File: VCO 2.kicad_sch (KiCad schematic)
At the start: 84 parts, among them J1 OUT 1x4s, J16 OCT_SW 1x7s, J18 CV 1x6s, J20 CTRL 1x9s, J85 Eurorack 2x8hs, J9 IN 1x6s, Q1 2N3904, Q2 2N3904, U1 CEM3340, U2 TL074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

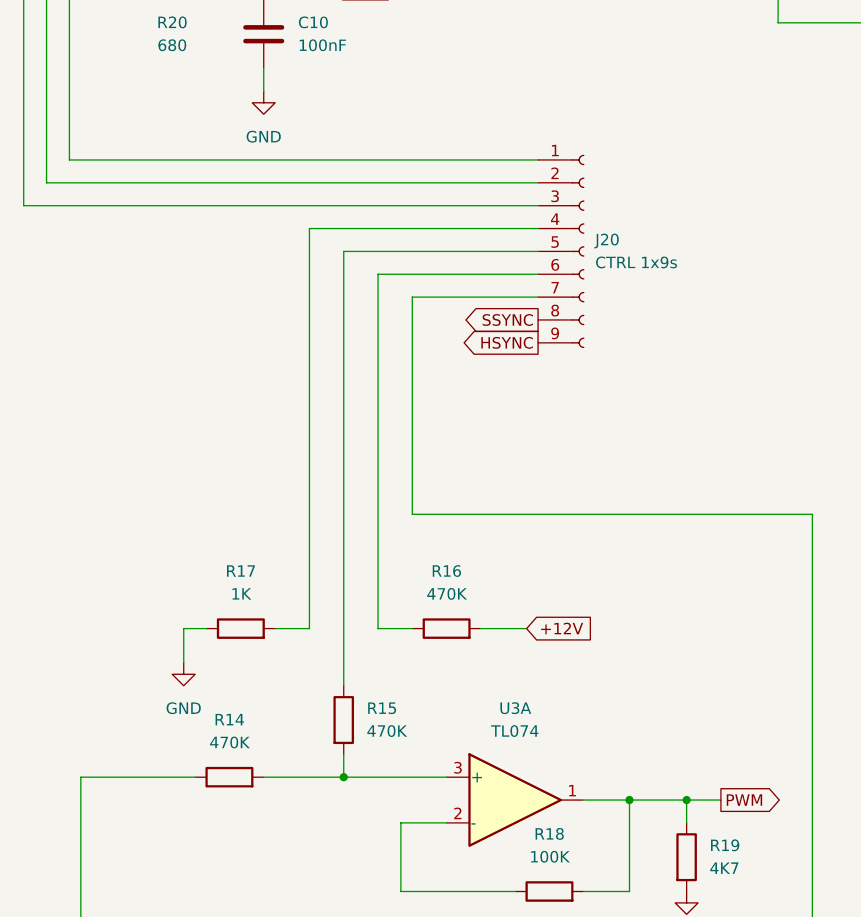
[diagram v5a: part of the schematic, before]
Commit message: Fixed FM sweep
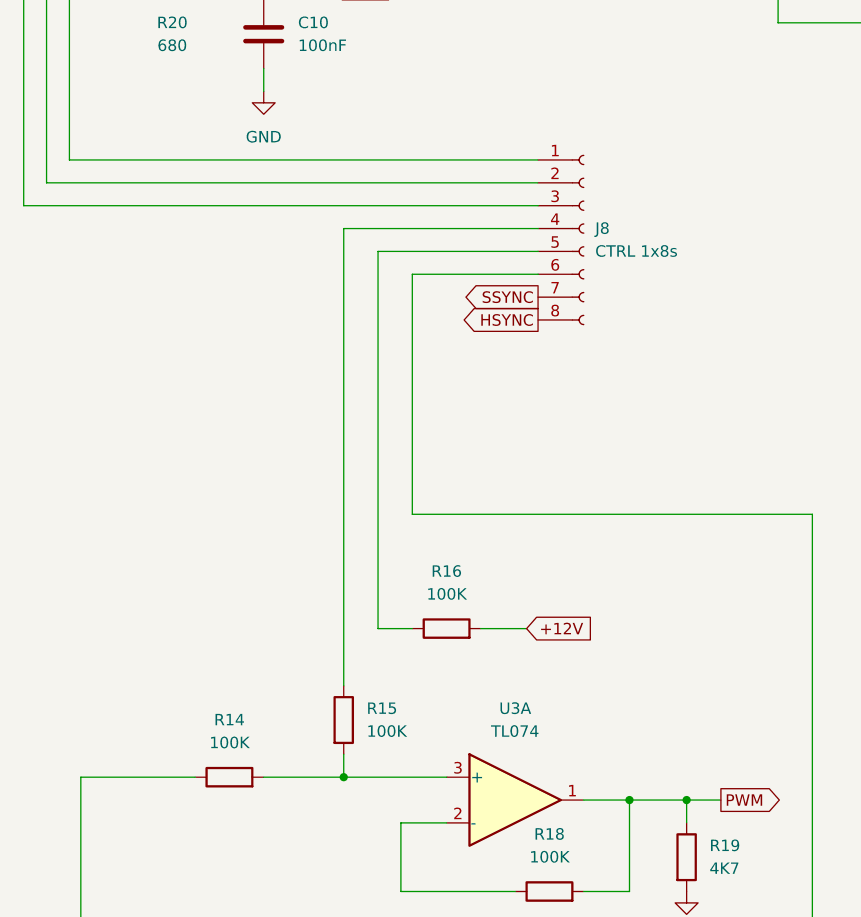
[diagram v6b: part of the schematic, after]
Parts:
- removed J20: CTRL 1x9s, Connector_PinSocket_2.54mm:PinSocket_1x09_P2.54mm_Vertical, symbol Connector:Conn_01x09_Socket
- removed R17: 1K, Resistor_THT:R_Axial_DIN0204_L3.6mm_D1.6mm_P7.62mm_Horizontal, symbol Device:R
- added J8: CTRL 1x8s, symbol Connector:Conn_01x08_Socket
- R14, R15, R16: value 470K -> 100K
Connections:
- net HSYNC: now also J8.8 (Pin_8)
- net SSYNC: now also J8.7 (Pin_7)
- net at R20.1, U1.3 (VEE): now also J8.1 (Pin_1)
- net at C6.1: now also J8.6 (Pin_6)
- net at R16.1: now also J8.5 (Pin_5)
- net at R1.1: now also J8.3 (Pin_3)
- net at R15.1: now also J8.4 (Pin_4)
- net at R2.1: now also J8.2 (Pin_2)
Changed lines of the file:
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@@
 	(wire
 		(pts
-			(xy 139.7 243.84) (xy 139.7 246.38)
+			(xy 78.74 113.03) (xy 64.77 113.03)
 		)
 		(stroke
@@
 	(wire
 		(pts
-			(xy 53.34 107.95) (xy 78.74 107.95)
+			(xy 139.7 243.84) (xy 139.7 246.38)
 		)
 		(stroke
@@
 	(wire
 		(pts
-			(xy 64.77 115.57) (xy 64.77 139.7)
-		)
-		(stroke
-			(width 0)
-			(type default)
-		)
-	)
-	(wire
-		(pts
 			(xy 194.31 53.34) (xy 194.31 52.07)
 		)
@@
 	(wire
 		(pts
-			(xy 39.37 152.4) (xy 39.37 156.21)
-		)
-		(stroke
-			(width 0)
-			(type default)
-		)
-	)
-	(wire
-		(pts
 			(xy 99.06 171.45) (xy 95.25 171.45)
 		)
@@
 	(wire
 		(pts
-			(xy 60.96 113.03) (xy 78.74 113.03)
-		)
-		(stroke
-			(width 0)
-			(type default)
-		)
-	)
-	(wire
-		(pts
 			(xy 105.41 78.74) (xy 109.22 78.74)
 		)
@@
 	(wire
 		(pts
-			(xy 41.91 152.4) (xy 39.37 152.4)
-		)
-		(stroke
-			(width 0)
-			(type default)
-		)
-	)
-	(wire
-		(pts
 			(xy 306.07 44.45) (xy 309.88 44.45)
 		)
@@
 	(wire
 		(pts
-			(xy 53.34 107.95) (xy 53.34 152.4)
-		)
-		(stroke
-			(width 0)
-			(type default)
-		)
-	)
-	(wire
-		(pts
 			(xy 215.9 260.35) (xy 215.9 262.89)
 		)
@@
 	(wire
 		(pts
+			(xy 78.74 107.95) (xy 57.15 107.95)
+		)
+		(stroke
+			(width 0)
+			(type default)
+		)
+	)
+	(wire
+		(pts
 			(xy 204.47 170.18) (xy 207.01 170.18)
 		)
@@
 	(wire
 		(pts
-			(xy 57.15 110.49) (xy 57.15 158.75)
+			(xy 57.15 107.95) (xy 57.15 158.75)
 		)
 		(stroke
@@
 	(wire
 		(pts
-			(xy 64.77 115.57) (xy 78.74 115.57)
+			(xy 201.93 270.51) (xy 201.93 274.32)
 		)
 		(stroke
@@
 	(wire
 		(pts
-			(xy 201.93 270.51) (xy 201.93 274.32)
+			(xy 105.41 38.1) (xy 129.54 38.1)
 		)
 		(stroke
@@
 	(wire
 		(pts
-			(xy 105.41 38.1) (xy 129.54 38.1)
+			(xy 179.07 170.18) (xy 181.61 170.18)
 		)
 		(stroke
@@
 	(wire
 		(pts
-			(xy 179.07 170.18) (xy 181.61 170.18)
+			(xy 271.78 226.06) (xy 245.11 226.06)
 		)
 		(stroke
@@
 	(wire
 		(pts
-			(xy 271.78 226.06) (xy 245.11 226.06)
+			(xy 64.77 113.03) (xy 64.77 139.7)
 		)
 		(stroke
@@
 	(wire
 		(pts
-			(xy 49.53 152.4) (xy 53.34 152.4)
-		)
-		(stroke
-			(width 0)
-			(type default)
-		)
-	)
-	(wire
-		(pts
 			(xy 215.9 257.81) (xy 215.9 260.35)
 		)
@@
 	(wire
 		(pts
-			(xy 60.96 113.03) (xy 60.96 152.4)
+			(xy 60.96 110.49) (xy 60.96 152.4)
 		)
 		(stroke
@@
 	(wire
 		(pts
-			(xy 57.15 110.49) (xy 78.74 110.49)
-		)
-		(stroke
-			(width 0)
-			(type default)
-		)
-	)
-	(wire
-		(pts
 			(xy 83.82 50.8) (xy 109.22 50.8)
 		)
@@
 	(wire
 		(pts
+			(xy 78.74 110.49) (xy 60.96 110.49)
+		)
+		(stroke
+			(width 0)
+			(type default)
+		)
+	)
+	(wire
+		(pts
 			(xy 187.96 52.07) (xy 187.96 57.15)
 		)
@@
 	(global_label "HSYNC"
 		(shape output)
-		(at 78.74 120.65 180)
+		(at 78.74 118.11 180)
 		(fields_autoplaced yes)
 		(effects
@@
 		)
 		(property "Intersheetrefs" "${INTERSHEET_REFS}"
-			(at 69.5257 120.65 0)
+			(at 69.5257 118.11 0)
 			(effects
 				(font
@@
 	(global_label "SSYNC"
 		(shape output)
-		(at 78.74 118.11 180)
+		(at 78.74 115.57 180)
 		(fields_autoplaced yes)
 		(effects
@@
 		)
 		(property "Intersheetrefs" "${INTERSHEET_REFS}"
-			(at 69.6467 118.11 0)
+			(at 69.6467 115.57 0)
 			(effects
 				(font
@@
 			)
 		)
-		(property "Value" "470K"
+		(property "Value" "100K"
 			(at 68.58 148.59 90)
 			(effects
@@
 	)
 	(symbol
-		(lib_id "power:GND")
-		(at 39.37 156.21 0)
-		(unit 1)
-		(exclude_from_sim no)
-		(in_bom yes)
-		(on_board yes)
-		(dnp no)
-		(fields_autoplaced yes)
-		(property "Reference" "#PWR024"
-			(at 39.37 162.56 0)
-			(effects
-				(font
-					(size 1.27 1.27)
-				)
-				(hide yes)
-			)
-		)
-		(property "Value" "GND"
-			(at 39.37 161.29 0)
-			(effects
-				(font
-					(size 1.27 1.27)
-				)
-			)
-		)
-		(property "Footprint" ""
-			(at 39.37 156.21 0)
-			(effects
-				(font
-					(size 1.27 1.27)
-				)
-				(hide yes)
-			)
-		)
-		(property "Datasheet" ""
-			(at 39.37 156.21 0)
-			(effects
-				(font
-					(size 1.27 1.27)
-				)
-				(hide yes)
-			)
-		)
-		(property "Description" "Power symbol creates a global label with name \"GND\" , ground"
-			(at 39.37 156.21 0)
-			(effects
-				(font
-					(size 1.27 1.27)
-				)
-				(hide yes)
-			)
-		)
-		(pin "1"
-		)
-		(instances
-			(project ""
-				(path "/eb1652b6-57da-4a0e-88a4-449907a19840"
-					(reference "#PWR024")
-					(unit 1)
-				)
-			)
-		)
-	)
-	(symbol
 		(lib_id "Device:R")
 		(at 39.37 38.1 90)
@@
 			)
 		)
-		(property "Value" "470K"
+		(property "Value" "100K"
 			(at 59.69 163.8299 0)
 			(effects
@@
 	)
 	(symbol
-		(lib_id "Connector:Conn_01x09_Socket")
-		(at 83.82 110.49 0)
-		(unit 1)
-		(exclude_from_sim no)
-		(in_bom yes)
-		(on_board yes)
-		(dnp no)
-		(fields_autoplaced yes)
-		(property "Reference" "J20"
-			(at 85.09 109.2199 0)
-			(effects
-				(font
-					(size 1.27 1.27)
-				)
-				(justify left)
-			)
-		)
-		(property "Value" "CTRL 1x9s"
-			(at 85.09 111.7599 0)
-			(effects
-				(font
-					(size 1.27 1.27)
-				)
-				(justify left)
-			)
-		)
-		(property "Footprint" "Connector_PinSocket_2.54mm:PinSocket_1x09_P2.54mm_Vertical"
-			(at 83.82 110.49 0)
-			(effects
-				(font
-					(size 1.27 1.27)
-				)
-				(hide yes)
-			)
-		)
-		(property "Datasheet" "~"
-			(at 83.82 110.49 0)
-			(effects
-				(font
-					(size 1.27 1.27)
-				)
-				(hide yes)
-			)
-		)
-		(property "Description" "Generic connector, single row, 01x09, script generated"
-			(at 83.82 110.49 0)
-			(effects
-				(font
-					(size 1.27 1.27)
-				)
-				(hide yes)
-			)
-		)
-		(pin "6"
-		)
-		(pin "4"
-		)
-		(pin "3"
-		)
-		(pin "2"
-		)
-		(pin "5"
-		)
-		(pin "7"
-		)
-		(pin "1"
-		)
-		(pin "9"
-		)
-		(pin "8"
-		)
-		(instances
-			(project ""
-				(path "/eb1652b6-57da-4a0e-88a4-449907a19840"
-					(reference "J20")
-					(unit 1)
-				)
-			)
-		)
-	)
-	(symbol
 		(lib_id "Device:C")
 		(at 100.33 267.97 0)
@@
 	)
 	(symbol
-		(lib_id "Device:R")
-		(at 45.72 152.4 90)
+		(lib_id "Connector:Conn_01x08_Socket")
+		(at 83.82 107.95 0)
 		(unit 1)
 		(exclude_from_sim no)
@@
 		(dnp no)
 		(fields_autoplaced yes)
-		(property "Reference" "R17"
-			(at 45.72 146.05 90)
+		(property "Reference" "J8"
+			(at 85.09 107.9499 0)
 			(effects
 				(font
 					(size 1.27 1.27)
 				)
+				(justify left)
 			)
 		)
-		(property "Value" "1K"
-			(at 45.72 148.59 90)
+		(property "Value" "CTRL 1x8s"
+			(at 85.09 110.4899 0)
 			(effects
 				(font
 					(size 1.27 1.27)
 				)
+				(justify left)
 			)
 		)
-		(property "Footprint" "Resistor_THT:R_Axial_DIN0204_L3.6mm_D1.6mm_P7.62mm_Horizontal"
-			(at 45.72 154.178 90)
+		(property "Footprint" ""
+			(at 83.82 107.95 0)
 			(effects
 				(font
@@
 		)
 		(property "Datasheet" "~"
-			(at 45.72 152.4 0)
+			(at 83.82 107.95 0)
 			(effects
 				(font
@@
 			)
 		)
-		(property "Description" "Resistor"
-			(at 45.72 152.4 0)
+		(property "Description" "Generic connector, single row, 01x08, script generated"
+			(at 83.82 107.95 0)
 			(effects
 				(font
@@
 			)
 		)
-		(pin "1"
+		(pin "6"
+		)
+		(pin "5"
+		)
+		(pin "3"
+		)
+		(pin "4"
 		)
 		(pin "2"
 		)
+		(pin "7"
+		)
+		(pin "8"
+		)
+		(pin "1"
+		)
 		(instances
-			(project "VCO 2"
+			(project ""
 				(path "/eb1652b6-57da-4a0e-88a4-449907a19840"
-					(reference "R17")
+					(reference "J8")
 					(unit 1)
 				)
@@
 			)
 		)
-		(property "Value" "470K"
+		(property "Value" "100K"
 			(at 44.45 165.1 90)
 			(effects

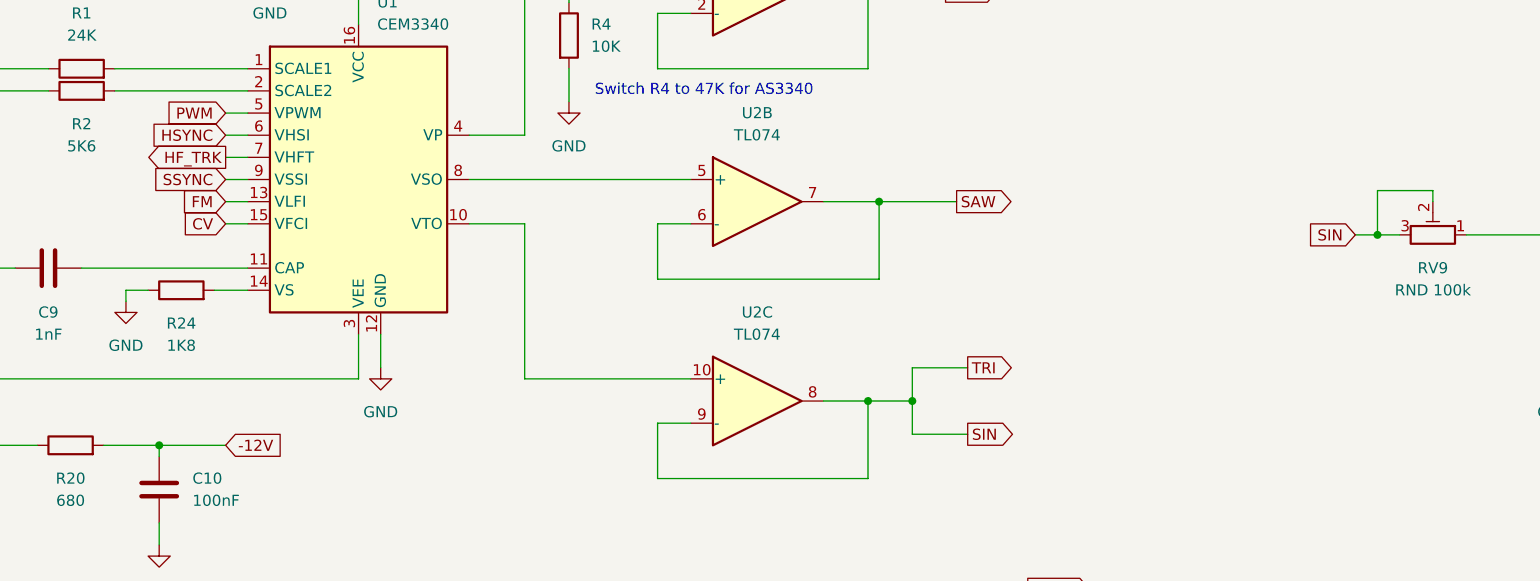
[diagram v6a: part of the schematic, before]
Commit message: Added decoupling C and R to prevent MacArches
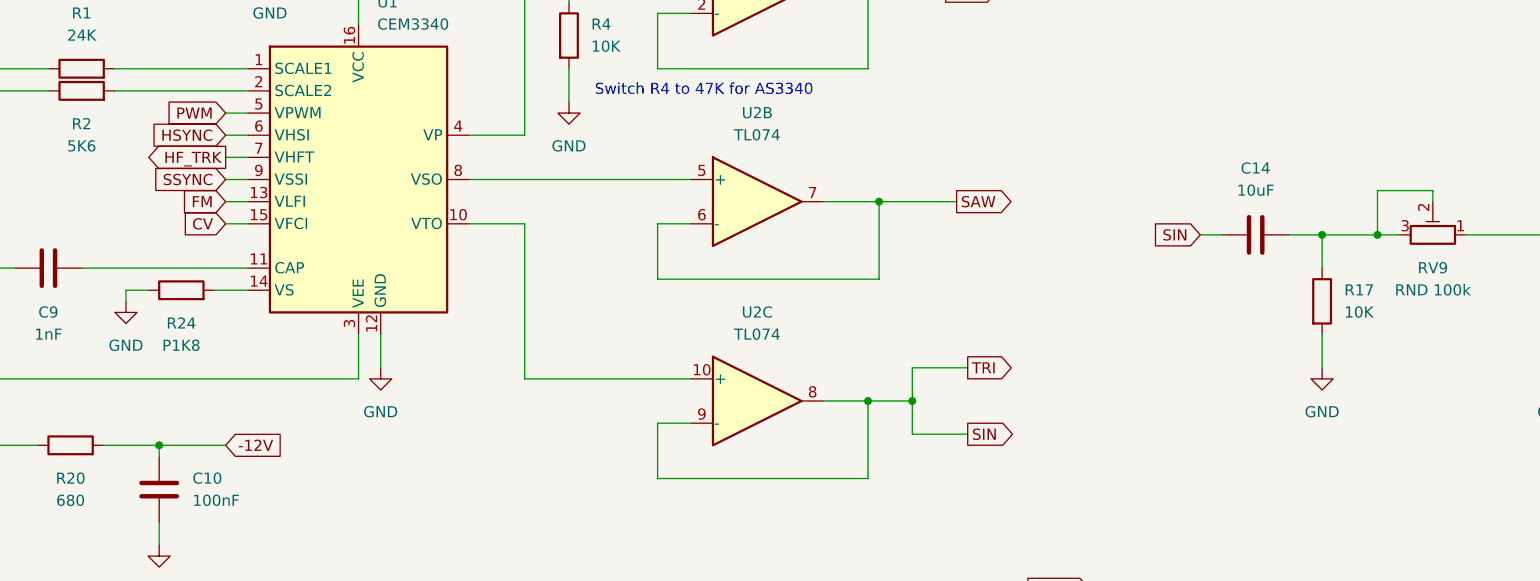
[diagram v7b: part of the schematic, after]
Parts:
- added C14: 10uF, symbol Device:C
- added R17: 10K, symbol Device:R
- R24: value 1K8 -> P1K8
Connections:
- net GND: now also R17.2
- net SIN: now also C14.2; no longer RV9.2, RV9.3
- new net: C14.1, R17.1, RV9.2, RV9.3

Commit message: Added gain and 1k protection to output and LED, rerouted SIN feed.
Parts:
- added D1: LED, symbol Device:LED
- added R43, R44, R45, R46, R47, R48: 1K, symbol Device:R
- added R49: 220R, symbol Device:R
- added R50: 1K5, symbol Device:R
- added R51: 470R, symbol Device:R
- added TP2: SQR, TestPoint:TestPoint_Loop_D2.50mm_Drill1.0mm, symbol Connector:TestPoint
- added TP3: SAW, TestPoint:TestPoint_Loop_D2.50mm_Drill1.0mm, symbol Connector:TestPoint
- added TP4: TRI, TestPoint:TestPoint_Loop_D2.50mm_Drill1.0mm, symbol Connector:TestPoint
- added TP5: SIN, TestPoint:TestPoint_Loop_D2.50mm_Drill1.0mm, symbol Connector:TestPoint
- R10, R22, R34, R5: value 470 -> 470R
- R20: value 680 -> 680R
- R42: value 510 -> 510R
- R73, R74: value 10 -> 10R
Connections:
- net +12V: now also D1.2 (A)
- net GND: now also R46.1, R47.1, R51.2
- net SAW: now also R44.2, TP3.1; no longer U2.6 (-), U2.7
- net SIN: now also U1.10 (VTO), U2.10 (+); no longer J1.3 (Pin_3), U2.8, U2.9 (-)
- net SQR: now also R43.2, TP2.1; no longer U2.1, U2.2 (-)
- net at R11.2, U2.14: now also R48.1; no longer J1.4 (Pin_4)
- new net: R45.1, R50.2, U2.8
- new net: R46.2, R50.1, U2.9 (-)
- new net: R47.2, R49.1, U2.6 (-)
- new net: R44.1, R49.2, U2.7
- new net: J1.4 (Pin_4), R48.2, TP5.1
- new net: R43.1, U2.1, U2.2 (-)
- new net: D1.1 (K), R51.1
- new net TRI: J1.3 (Pin_3), R45.2, TP4.1
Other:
- moved on the sheet: C1, C12, C2, D11, J16, J18, R25, R26, R27, R28, R29, R3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
